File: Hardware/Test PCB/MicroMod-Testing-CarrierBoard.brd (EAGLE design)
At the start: 61 x 40.6 mm, 118 parts, among them J11 microSD, J12 SPI, J14 I2C, J2 JTAG, J3 QWIIC_RIGHT_ANGLE, J5 UART, J6 MICROMOD-2222-C, J8 Dedicated, U2 MCP73831, U5 AP7361C-33

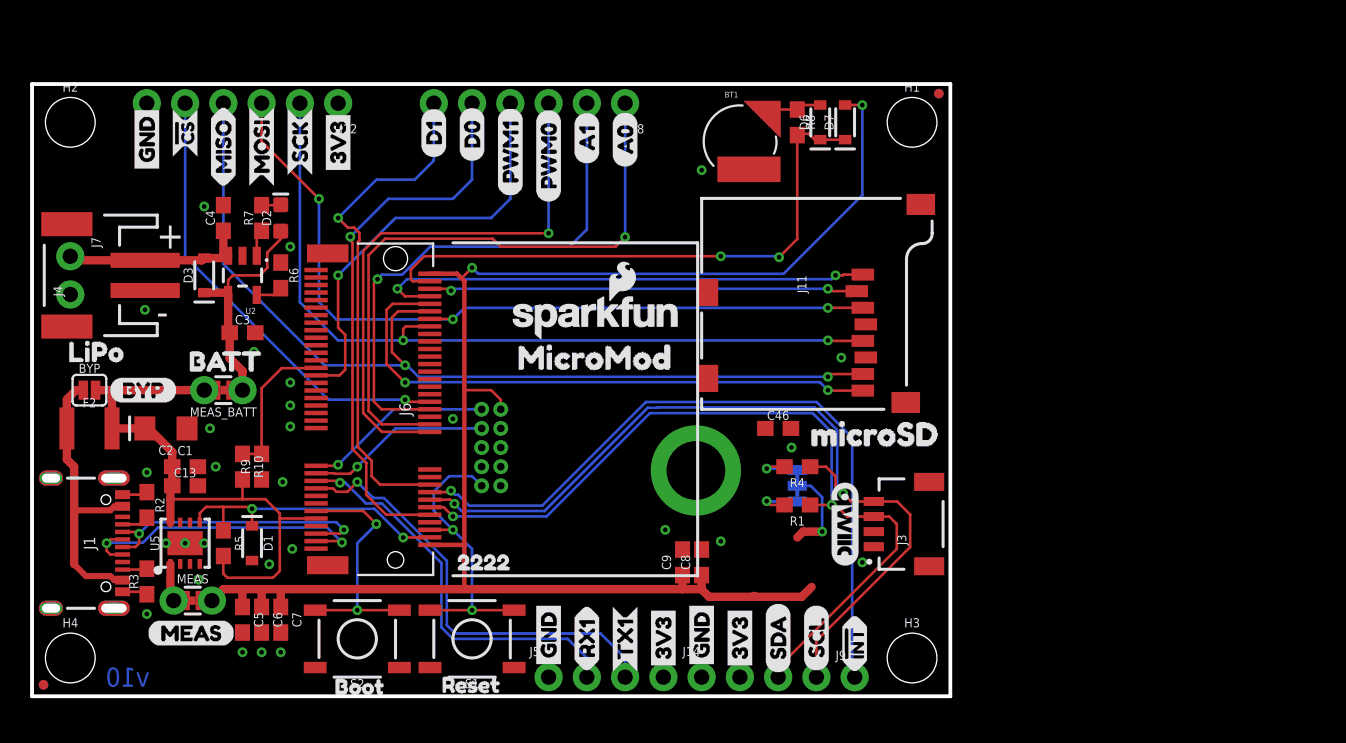
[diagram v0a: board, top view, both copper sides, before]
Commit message: Finishes trace work on Test board - needs some silk
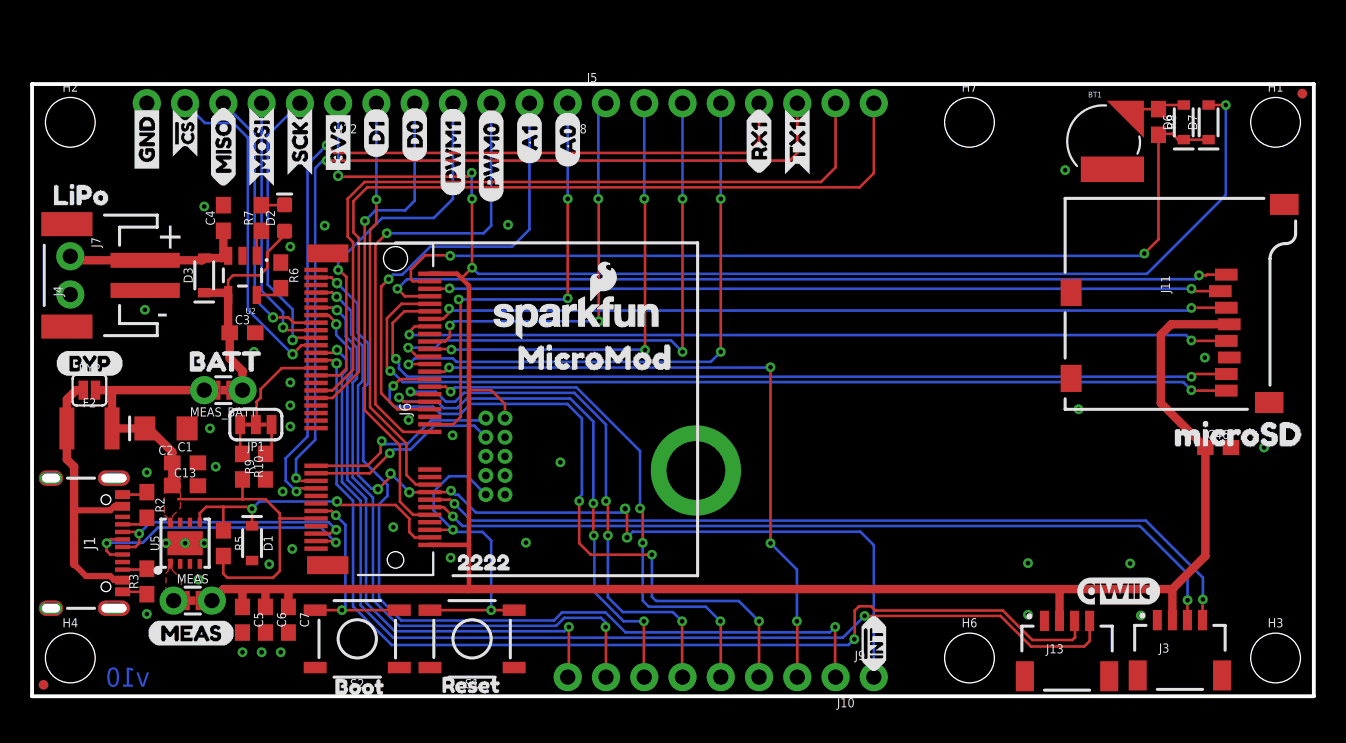
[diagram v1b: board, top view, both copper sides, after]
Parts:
- removed C8: 10uF, SparkFun-Capacitors:0603
- removed C9: 1.0uF, SparkFun-Capacitors:0603
- removed J14: I2C, SparkFun-Connectors:1X04_NO_SILK
- removed R1, R4: 2.2k, SparkFun-Resistors:0603
- removed U$17, U$20, U$38, U$46: (no value), SparkFun-Buzzard:3V3_P
- removed U$18: (no value), SparkFun-Buzzard:JTAG_TO
- removed U$32, U$36, U$42, U$45: (no value), SparkFun-Buzzard:GND_P
- removed U$37: (no value), SparkFun-Buzzard:I2C
- removed U$39, U$47: (no value), SparkFun-Buzzard:SDA_IO
- removed U$40, U$48: (no value), SparkFun-Buzzard:SCL_IO
- added H6, H7: STAND-OFF, SparkFun-Hardware:STAND-OFF
- added J10: (no value), SparkFun-Connectors:1X08_NO_SILK
- added J13: QWIIC_RIGHT_ANGLE, SparkFun-Connectors:JST04_1MM_RA
- J5: value UART -> (none); device SparkFun-Connectors:1X04_NO_SILK -> SparkFun-Connectors:1X08_NO_SILK
- JP1: value (none) -> JUMPER-SMT_3_2-NC_TRACE_SILK
- moved J5 38.3 mm to (38.1, 39.4)
- moved JP1 36.2 mm to (14.9, 18.0), flipped to the top, turned to 180 degrees
- moved U$25 34.9 mm to (48.3, 34.7)
- moved U$29 34.9 mm to (48.3, 34.7)
- moved U$31 34.9 mm to (50.8, 34.5)
- moved U$41 34.9 mm to (50.8, 34.5)
- moved C46 29.2 mm to (78.7, 16.5)
- moved BT1 24.1 mm to (71.1, 36.8)
- moved D7 24.1 mm to (78.1, 38.1)
- moved FD2 24.1 mm to (84.3, 40.0)
- moved FD4 24.1 mm to (84.3, 40.0)
- moved D6 24.1 mm to (76.5, 38.1)
- moved H1 24.1 mm to (82.5, 38.1)
- moved H3 24.1 mm to (82.5, 2.54)
- moved J11 24.1 mm to (68.6, 19.1)
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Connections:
- net N$1 renamed OUT_MEAS
- removed net HEADER_!CS!: J12.5, J6.40
- removed net I2C_!INT!: J6.16, J9.1
- removed net I2C_SCL: J14.4, J3.4, J6.14, R4.1
- removed net I2C_SDA: J14.3, J3.3, J6.12, R1.1
- new net !CS1: J12.5, J6.55
- new net A5: J10.7, J6.65
- new net A6: J10.8, J6.63
- new net CAN_RXI: J5.8, J6.41
- new net CAN_TXO: J5.7, J6.43
- new net D2: J10.6, J6.40
- new net D3: J10.5, J6.42
- new net D4: J10.4, J6.44
- new net D5: J10.3, J6.46
- new net D6: J10.2, J6.48
- new net D7: J10.1, J6.73
- new net D8/!INT: J6.16, J6.69, J9.1
- new net I2S_CLK: J5.4, J6.50
- new net I2S_SDI: J5.2, J6.54
- new net I2S_SDO: J5.1, J6.56
- new net I2S_WS: J5.3, J6.52
- new net MISO1: J12.4, J6.61
- new net MOSI1: J12.3, J6.59
- new net SCL: J3.4, J6.14
- new net SCL1: J13.4, J6.53
- new net SCLK1: J12.2, J6.57
- new net SDA: J3.3, J6.12
- new net SDA1: J13.3, J6.51
- net 3.3V: now also J13.2; no longer C8.1, C9.1, J14.2, J5.4, JP1.2
- net GND: now also J13.1; no longer C8.2, C9.2, J14.1, J5.1
- net N$2: now also R10.1; no longer R4.2
- net N$3: now also R9.2; no longer R1.2
- net RX1: now also J5.6; no longer J5.2
- net SPI_MISO: no longer J12.4
- net SPI_MOSI: no longer J12.3
- net SPI_SCK: no longer J12.2
- net TX1: now also J5.5; no longer J5.3
- net VIN/3: now also JP1.2; no longer R10.1, R9.2
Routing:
- net 3.3V: track 117.8 -> 206.4 mm, vias 3 -> 5
- net SCL1: track 0.00 -> 71.5 mm, vias 0 -> 2
- net SDA1: track 0.00 -> 71.3 mm, vias 0 -> 2
- net D8/!INT: track 0.00 -> 61.8 mm, vias 0 -> 7
- net D7: track 0.00 -> 59.5 mm, vias 0 -> 2
- net I2C_SCL: track 56.9 -> 0.00 mm, vias 2 -> 0
- net SCL: track 0.00 -> 56.3 mm, vias 0 -> 2
- net SDA: track 0.00 -> 55.2 mm, vias 0 -> 2
- net CAN_RXI: track 0.00 -> 55.0 mm
- net I2C_SDA: track 54.8 -> 0.00 mm, vias 2 -> 0
- net CAN_TXO: track 0.00 -> 52.0 mm
- net I2C_!INT!: track 48.3 -> 0.00 mm, vias 1 -> 0
- net D5: track 0.00 -> 45.3 mm, vias 0 -> 4
- net D6: track 0.00 -> 44.0 mm, vias 0 -> 4
- net A5: track 0.00 -> 42.1 mm, vias 0 -> 2
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- added copper zone on layer 1, net OUT_MEAS
- added copper zone on layer 1, net VIN
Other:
- board size 61 x 40.6 mm -> 85.1 x 40.6 mm

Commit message: Adds silk to Testbed and moves SWD header
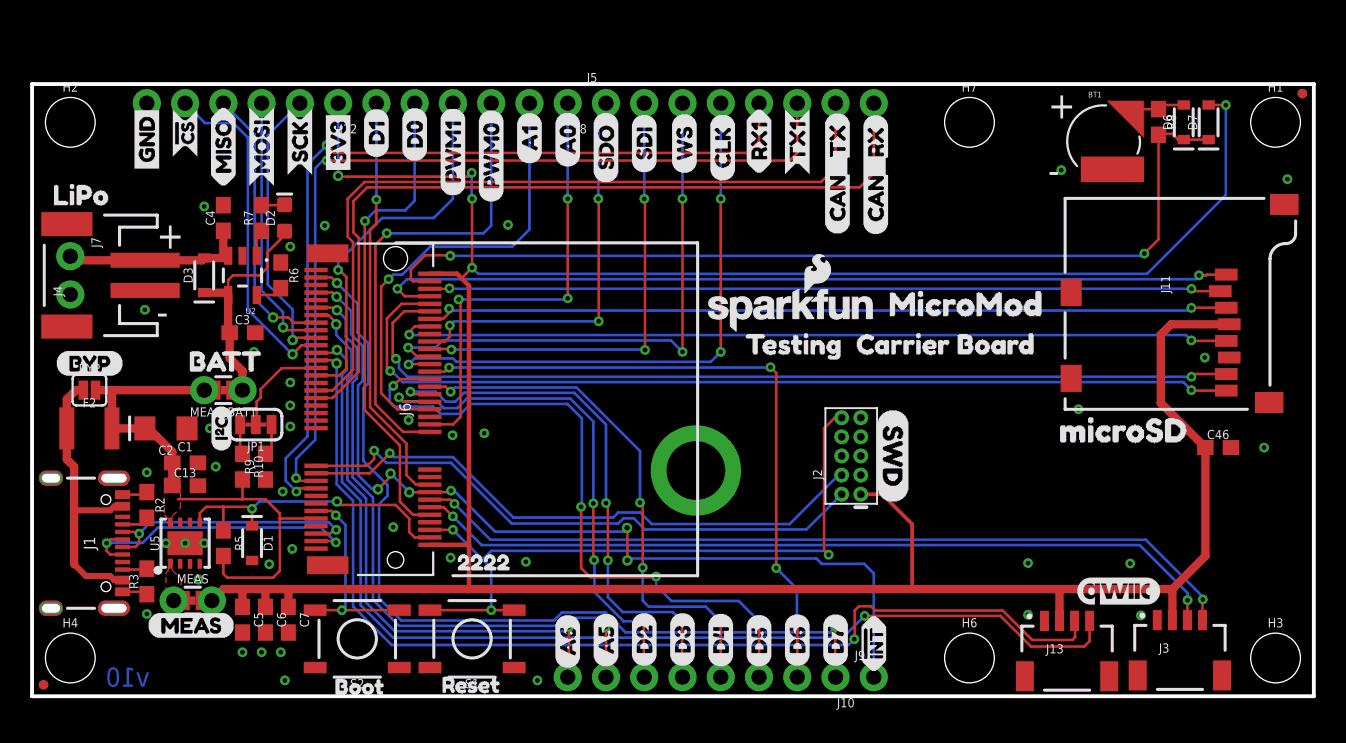
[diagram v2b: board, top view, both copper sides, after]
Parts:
- added U$1: (no value), bottom PTH:A51
- added U$11: (no value), bottom PTH:D22
- added U$17: (no value), bottom PTH:D33
- added U$18: (no value), bottom PTH:D44
- added U$20: (no value), bottom PTH:D55
- added U$3: (no value), bottom PTH:A60
- added U$30: (no value), bottom PTH:D66
- added U$32: (no value), bottom PTH:D77
- added U$34: (no value), Top PTH:CAN_RX5
- added U$36: (no value), Top PTH:CAN_TX4
- added U$37: (no value), Top PTH:CLK3
- added U$38: (no value), Top PTH:SDI1
- added U$39: (no value), Top PTH:SDO0
- added U$40: (no value), Top PTH:WS2
- added U$42: (no value), SparkFun-Buzzard:I2C_32
- added U$45: (no value), Carrier Board:CARRIER_BOARD0
- added U$46: (no value), testing:TESTING0
- added U$47: (no value), SWD:SWD0
- moved U$24 24.9 mm to (55.5, 26.0)
- moved J2 23.6 mm to (54.4, 16.0), flipped to the top, turned to 90 degrees
- moved FRAME1 16.8 mm to (20.6, -10.7)
- moved LOGO1 14.2 mm to (50.4, 25.7)
- moved U$28 7.62 mm to (66.8, 17.7)
- moved U$5 0.51 mm to (7.62, 4.70)
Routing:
- net SWDCK: track 12.9 -> 39.0 mm
- net SWDIO: track 13.2 -> 39.1 mm
- net !RESET!: track 22.0 -> 46.8 mm, vias 2 -> 3
- net 3.3V: track 206.4 -> 211.3 mm
- net D8/!INT: track 61.8 -> 60.7 mm
- net SCL: track 56.3 -> 55.5 mm
- net SDA: track 55.2 -> 54.5 mm
- net GND: vias 37 -> 40

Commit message: Updates silk on testing carrier board
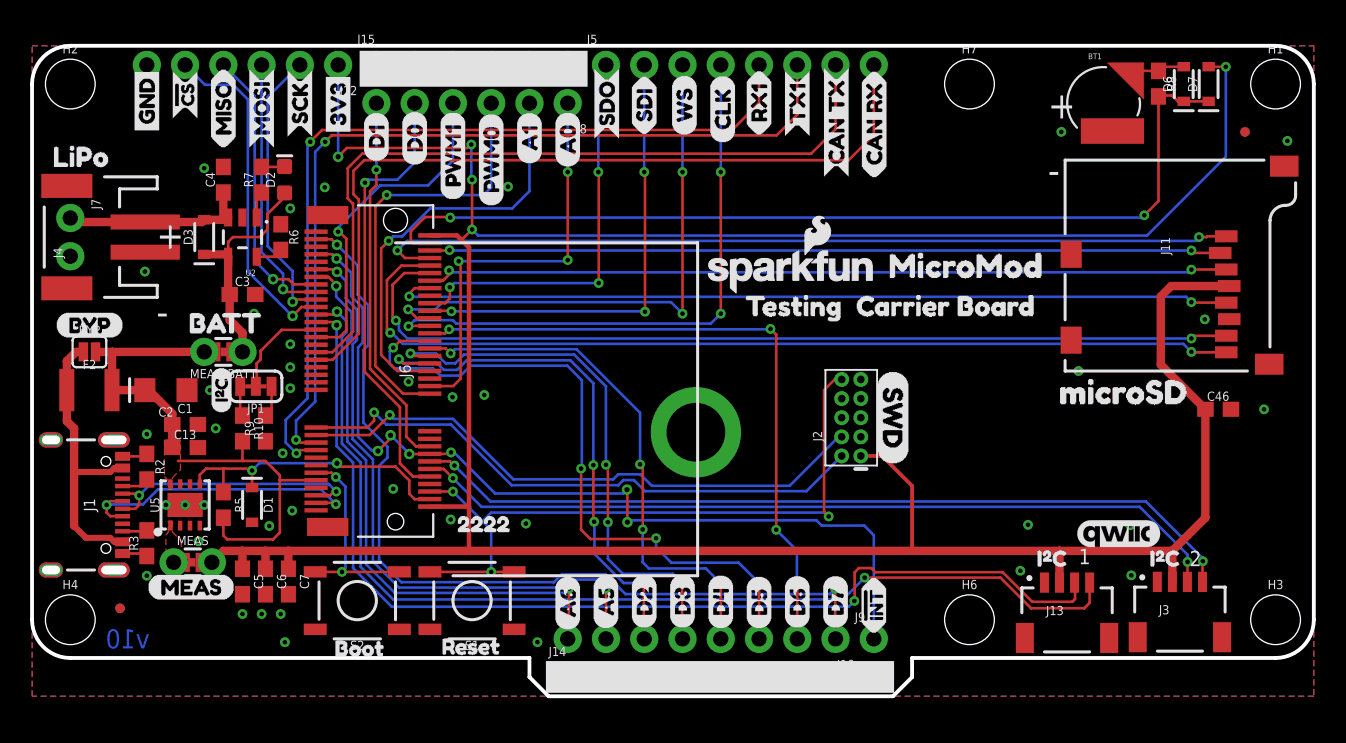
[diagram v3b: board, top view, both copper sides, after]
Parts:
- added J14: (no value), SparkFun-Connectors:1X09_NO_SILK
- added J15: Dedicated, SparkFun-Connectors:1X06_NO_SILK
- added U$48: (no value), Top PTH:CAN_RX2
- added U$54: (no value), Top PTH:CAN_TX3
- added U$62: (no value), Top PTH:CLK3
- added U$63: (no value), Top PTH:SDI1
- added U$65: (no value), Top PTH:SDO0
- added U$66: (no value), Top PTH:WS2
- added U$67: (no value), bottom PTH:A51
- added U$68: (no value), bottom PTH:A60
- added U$69: (no value), bottom PTH:D22
- added U$70: (no value), bottom PTH:D33
- added U$71: (no value), bottom PTH:D44
- added U$72: (no value), bottom PTH:D55
- added U$73: (no value), bottom PTH:D66
- added U$74: (no value), bottom PTH:D77
- added U$75, U$76: (no value), SparkFun-Buzzard:I2C_TO
- U$34: device Top PTH:CAN_RX5 -> Top PTH:CAN_RX2
- U$36: device Top PTH:CAN_TX4 -> Top PTH:CAN_TX3
- moved FD1 7.18 mm to (5.84, 5.84)
- moved FD3 7.18 mm to (5.84, 5.84)
- moved FD2 4.58 mm to (80.5, 37.5)
- moved FD4 4.58 mm to (80.5, 37.5)
- moved LOGO2 3.81 mm to (72.1, 10.8)
- moved U$36 3.79 mm to (53.4, 34.4)
- moved U$34 3.74 mm to (55.9, 34.3)
- moved U$39 2.92 mm to (38.2, 37.0)
- moved U$23 2.54 mm to (20.3, 37.1)
- moved U$31 2.54 mm to (50.8, 37.1)
- moved U$37 2.54 mm to (45.8, 36.7)
- moved U$41 2.54 mm to (50.8, 37.1)
- moved U$49 2.54 mm to (17.8, 37.1)
- moved U$50 2.54 mm to (15.2, 36.3)
- moved U$51 2.54 mm to (12.7, 36.3)
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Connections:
- net GND: now also J14.1, J14.2, J14.3, J14.4, J14.5, J14.6, J14.7, J14.8, J14.9, J15.1, J15.2, J15.3, J15.4, J15.5, J15.6
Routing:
- net PWM1: track 25.3 -> 22.6 mm
- net PWM0: track 31.3 -> 28.8 mm
- net D0: track 32.3 -> 29.7 mm
- net D1: track 27.7 -> 25.1 mm
- net A1: track 30.5 -> 28.0 mm
- net A0: track 30.3 -> 27.8 mm
- net TX1: track 57.6 -> 56.4 mm
- net RX1: track 58.2 -> 57.4 mm
- net 3.3V: track 211.3 -> 212.1 mm
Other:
- board size 85.1 x 40.6 mm -> 85.1 x 43.2 mm
- board text added: "1"
- board text added: "2"
